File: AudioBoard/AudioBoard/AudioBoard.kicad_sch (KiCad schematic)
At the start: 0 parts

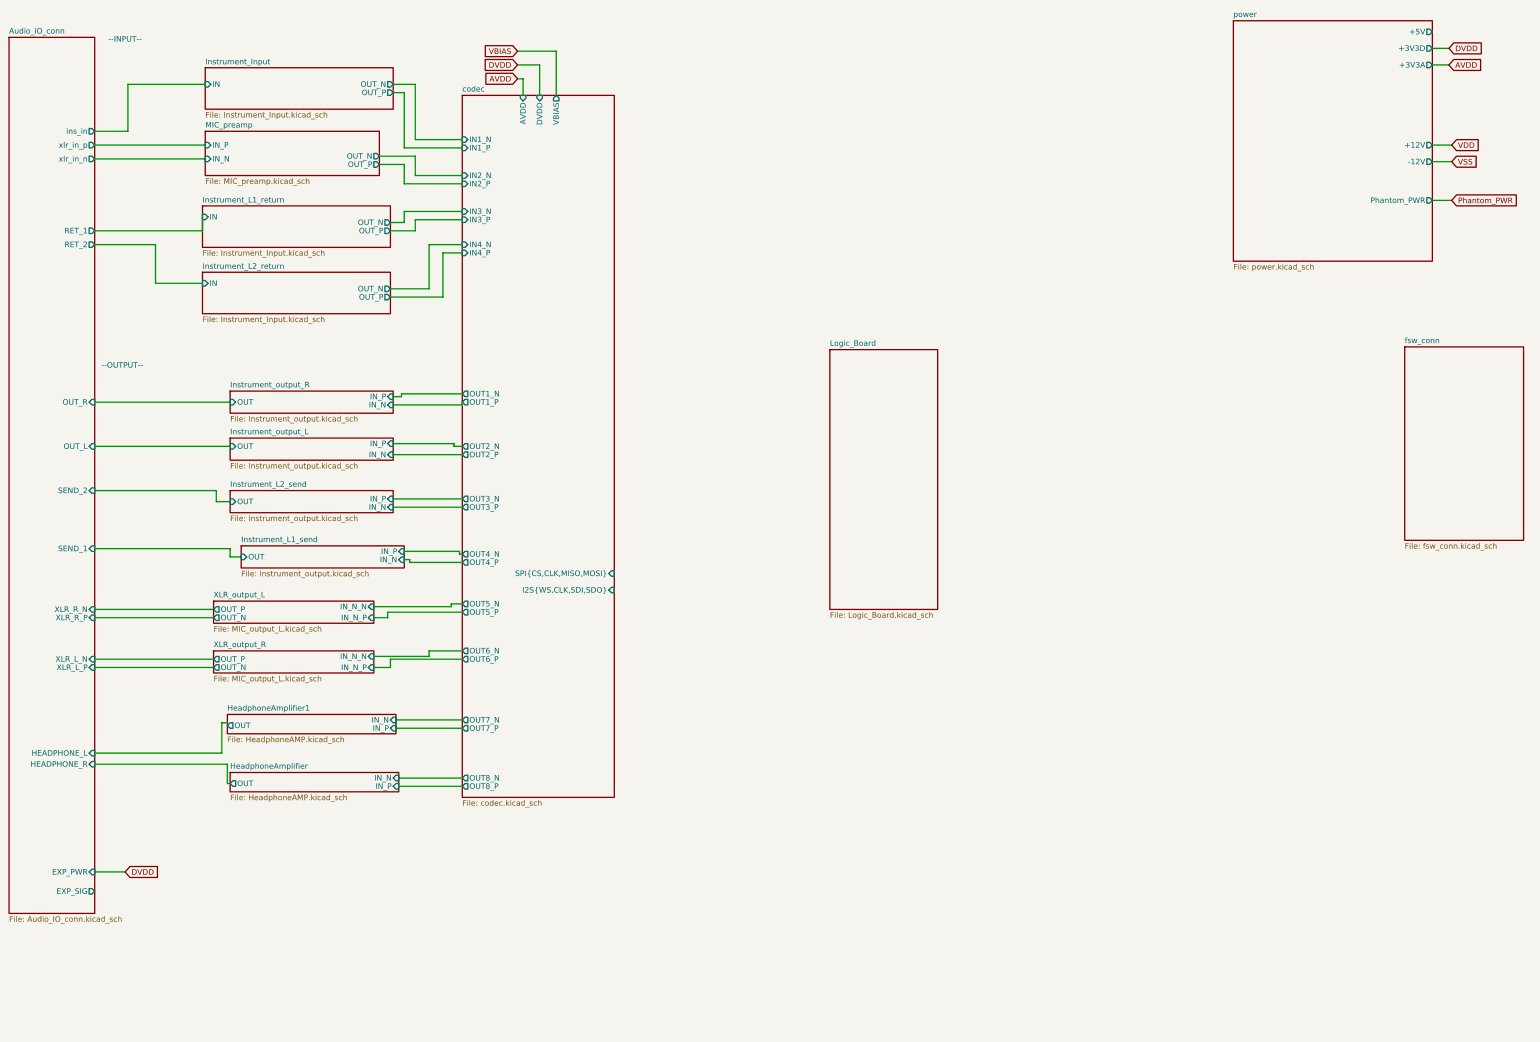
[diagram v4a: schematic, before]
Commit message: added bias voltage buffer, fixed fsw shift reg input filter
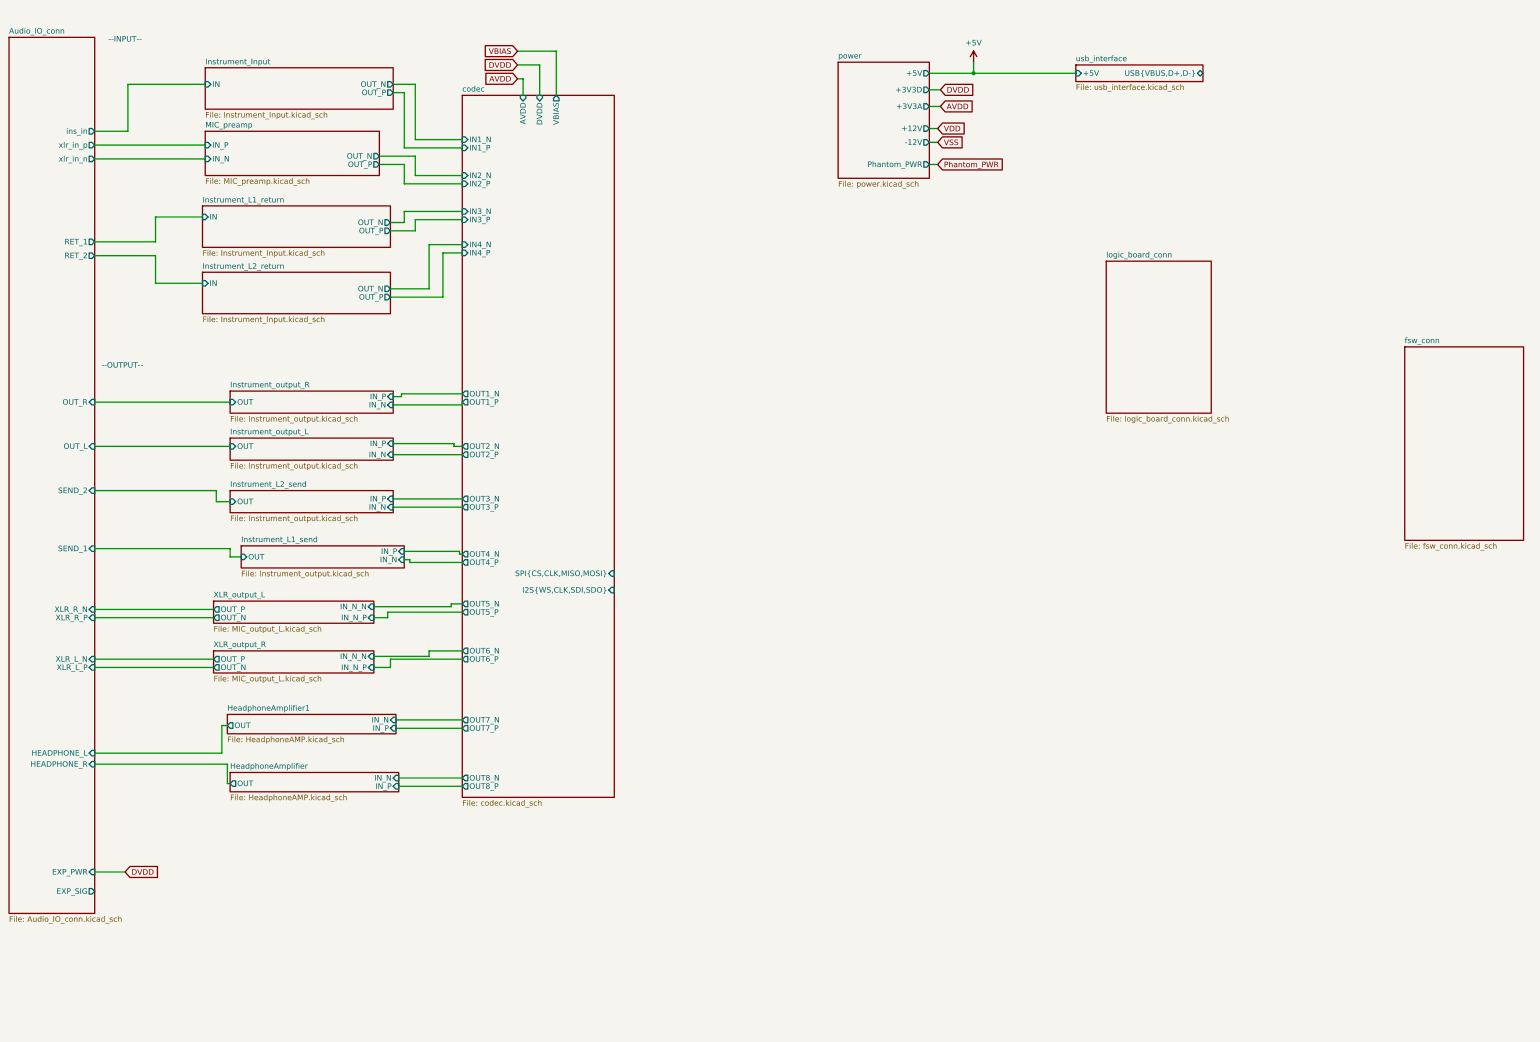
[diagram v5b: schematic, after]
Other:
- removed sheet Logic_Board
- added sheet logic_board_conn (logic_board_conn.kicad_sch)
- added sheet usb_interface (usb_interface.kicad_sch)

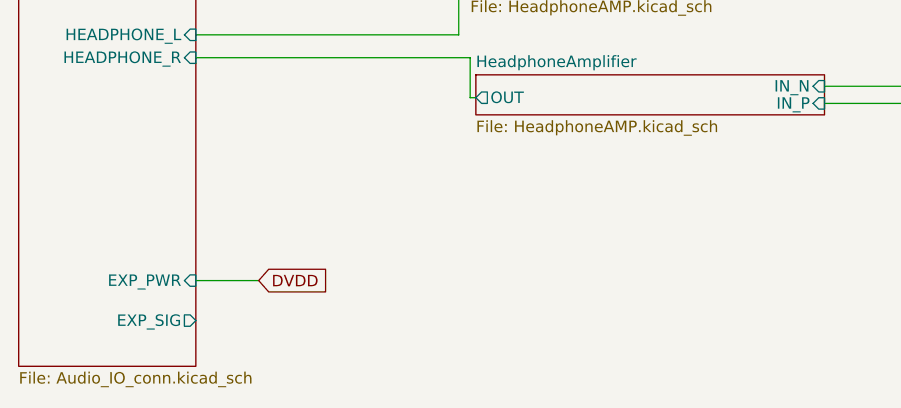
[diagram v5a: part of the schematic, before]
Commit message: modified clamping diodes on inputs, added exp pedal input filter, added ideas to instrument input filter redesign
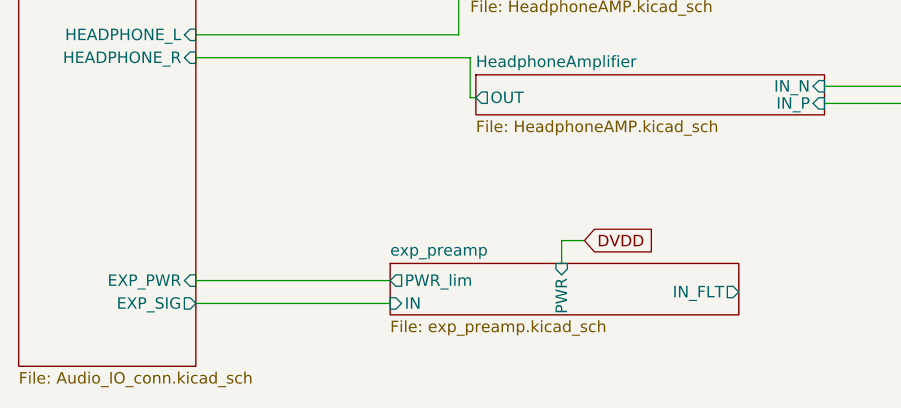
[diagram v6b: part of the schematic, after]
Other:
- added sheet exp_preamp (exp_preamp.kicad_sch)
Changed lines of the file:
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@@
 	(wire
 		(pts
-			(xy 60.325 215.9) (xy 53.34 215.9)
+			(xy 53.34 215.9) (xy 74.93 215.9)
 		)
 		(stroke
@@
 	(wire
 		(pts
+			(xy 93.98 211.455) (xy 93.98 213.995)
+		)
+		(stroke
+			(width 0)
+			(type default)
+		)
+	)
+	(wire
+		(pts
 			(xy 53.34 141.605) (xy 84.455 141.605)
 		)
@@
 	(wire
 		(pts
+			(xy 53.34 218.44) (xy 74.93 218.44)
+		)
+		(stroke
+			(width 0)
+			(type default)
+		)
+	)
+	(wire
+		(pts
 			(xy 245.11 40.005) (xy 247.65 40.005)
 		)
@@
 	(wire
 		(pts
+			(xy 96.52 211.455) (xy 93.98 211.455)
+		)
+		(stroke
+			(width 0)
+			(type default)
+		)
+	)
+	(wire
+		(pts
 			(xy 120.65 156.21) (xy 120.65 157.48)
 		)
@@
 			(width 0)
 			(type default)
-		)
-	)
-	(global_label "DVDD"
-		(shape input)
-		(at 60.325 215.9 0)
-		(fields_autoplaced yes)
-		(effects
-			(font
-				(size 1.27 1.27)
-			)
-			(justify left)
-		)
-		(property "Intersheetrefs" "${INTERSHEET_REFS}"
-			(at 68.2088 215.9 0)
-			(hide yes)
-			(show_name no)
-			(do_not_autoplace no)
-			(effects
-				(font
-					(size 1.27 1.27)
-				)
-				(justify left)
-			)
 		)
 	)
@@
 		(property "Intersheetrefs" "${INTERSHEET_REFS}"
 			(at 263.2442 53.34 0)
+			(hide yes)
+			(show_name no)
+			(do_not_autoplace no)
+			(effects
+				(font
+					(size 1.27 1.27)
+				)
+				(justify left)
+			)
+		)
+	)
+	(global_label "DVDD"
+		(shape input)
+		(at 96.52 211.455 0)
+		(fields_autoplaced yes)
+		(effects
+			(font
+				(size 1.27 1.27)
+			)
+			(justify left)
+		)
+		(property "Intersheetrefs" "${INTERSHEET_REFS}"
+			(at 104.4038 211.455 0)
 			(hide yes)
 			(show_name no)
@@
 		)
 		(pin "EXP_SIG" output
-			(at 53.34 220.345 0)
+			(at 53.34 218.44 0)
 			(effects
 				(font
@@
 				)
 			)
+		)
+	)
+	(sheet
+		(at 74.93 213.995)
+		(size 38.735 5.715)
+		(exclude_from_sim no)
+		(in_bom yes)
+		(on_board yes)
+		(dnp no)
+		(fields_autoplaced yes)
+		(stroke
+			(width 0.1524)
+			(type solid)
+		)
+		(fill
+			(color 0 0 0 0)
+		)
+		(property "Sheetname" "exp_preamp"
+			(at 74.93 213.2834 0)
+			(show_name no)
+			(do_not_autoplace no)
+			(effects
+				(font
+					(size 1.27 1.27)
+				)
+				(justify left bottom)
+			)
+		)
+		(property "Sheetfile" "exp_preamp.kicad_sch"
+			(at 74.93 220.2946 0)
+			(show_name no)
+			(do_not_autoplace no)
+			(effects
+				(font
+					(size 1.27 1.27)
+				)
+				(justify left top)
+			)
+		)
+		(pin "IN" input
+			(at 74.93 218.44 180)
+			(effects
+				(font
+					(size 1.27 1.27)
+				)
+				(justify left)
+			)
+		)
+		(pin "IN_FLT" output
+			(at 113.665 217.17 0)
+			(effects
+				(font
+					(size 1.27 1.27)
+				)
+				(justify right)
+			)
+		)
+		(pin "PWR" input
+			(at 93.98 213.995 90)
+			(effects
+				(font
+					(size 1.27 1.27)
+				)
+				(justify right)
+			)
+		)
+		(pin "PWR_lim" output
+			(at 74.93 215.9 180)
+			(effects
+				(font
+					(size 1.27 1.27)
+				)
+				(justify left)
+			)
+		)
+		(instances
+			(project "AudioBoard"
+				(path "/dd5d876d-fff7-4cb4-baee-a023036d12ae"
+					(page "20")
+				)
+			)
